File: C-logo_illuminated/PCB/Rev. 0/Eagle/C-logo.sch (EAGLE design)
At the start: 6 parts

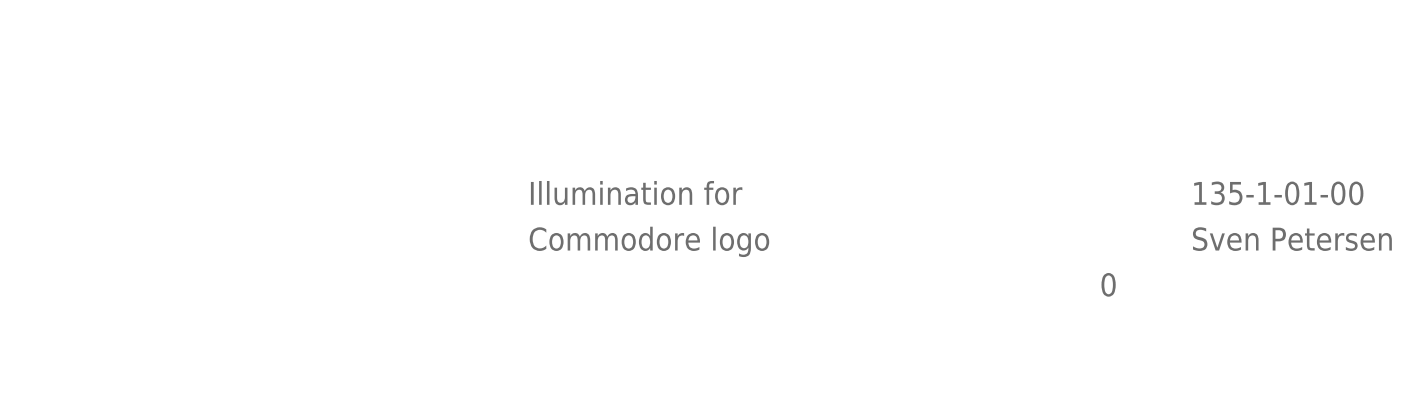
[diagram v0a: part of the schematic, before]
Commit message: Silk Screen updated
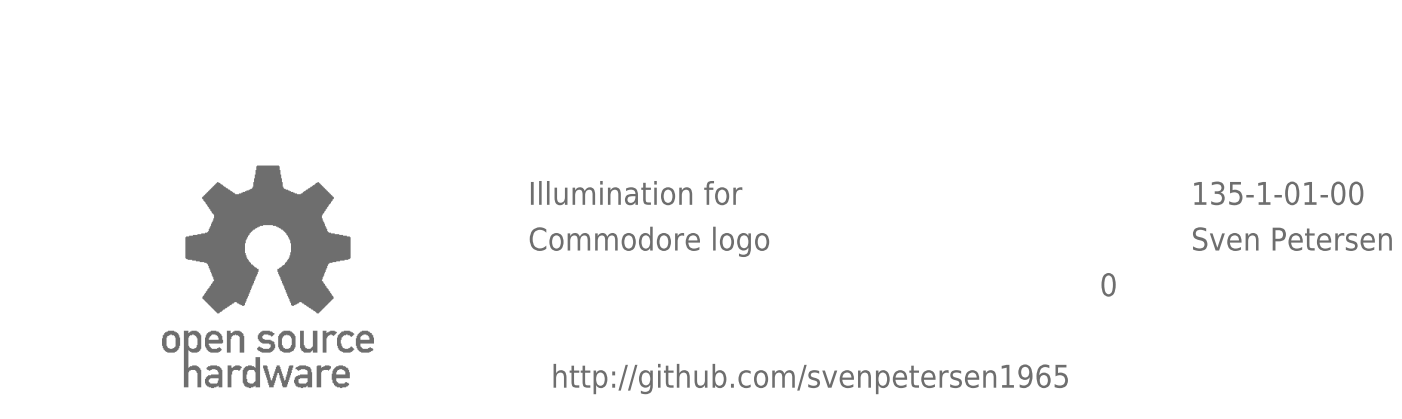
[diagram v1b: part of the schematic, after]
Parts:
- added U$5: OPEN_SOURCE_HW, Logo:OPEN_SOURCE_HW
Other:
- note added: "http://github.com/svenpetersen1965"
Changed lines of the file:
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@@
 <?xml version="1.0" encoding="utf-8"?>
 <!DOCTYPE eagle SYSTEM "eagle.dtd">
-<eagle version="9.2.2">
+<eagle version="9.5.2">
 <drawing>
 <settings>
@@
 <layer number="54" name="bGND_GNDA" color="7" fill="1" visible="no" active="no"/>
 <layer number="56" name="wert" color="7" fill="1" visible="no" active="no"/>
+<layer number="57" name="tCAD" color="7" fill="1" visible="no" active="no"/>
+<layer number="58" name="b3Ddata" color="7" fill="1" visible="no" active="no"/>
 <layer number="59" name="tCarbon" color="7" fill="1" visible="no" active="no"/>
 <layer number="60" name="bCarbon" color="7" fill="1" visible="no" active="no"/>
@@
 <layer number="97" name="Info" color="7" fill="1" visible="yes" active="yes"/>
 <layer number="98" name="Guide" color="6" fill="1" visible="yes" active="yes"/>
+<layer number="99" name="SpiceOrder" color="7" fill="1" visible="no" active="no"/>
 <layer number="100" name="Flex-Dim" color="1" fill="7" visible="no" active="no"/>
 <layer number="101" name="Flex-Kleb" color="1" fill="7" visible="no" active="no"/>
@@
 <layer number="115" name="logo4" color="7" fill="1" visible="yes" active="yes"/>
 <layer number="116" name="Patch_BOT" color="7" fill="1" visible="yes" active="yes"/>
+<layer number="117" name="BACKMAAT1" color="7" fill="1" visible="no" active="yes"/>
 <layer number="118" name="Rect_Pads" color="7" fill="1" visible="yes" active="yes"/>
+<layer number="119" name="KAP_TEKEN" color="7" fill="1" visible="no" active="yes"/>
+<layer number="120" name="120" color="7" fill="1" visible="no" active="yes"/>
 <layer number="121" name="_tsilk" color="7" fill="1" visible="yes" active="yes"/>
 <layer number="122" name="_bsilk" color="7" fill="1" visible="yes" active="yes"/>
@@
 <layer number="125" name="_tNames" color="7" fill="1" visible="no" active="no"/>
 <layer number="126" name="_bNames" color="7" fill="1" visible="no" active="no"/>
+<layer number="127" name="_tValues" color="7" fill="1" visible="no" active="yes"/>
+<layer number="128" name="_bValues" color="7" fill="1" visible="no" active="yes"/>
 <layer number="129" name="Mask" color="7" fill="1" visible="yes" active="yes"/>
+<layer number="130" name="SMDSTROOK" color="7" fill="1" visible="no" active="yes"/>
 <layer number="131" name="tAdjust" color="7" fill="1" visible="yes" active="yes"/>
 <layer number="132" name="bAdjust" color="7" fill="1" visible="yes" active="yes"/>
+<layer number="133" name="Ports" color="7" fill="1" visible="no" active="yes"/>
+<layer number="134" name="Port2" color="7" fill="1" visible="no" active="yes"/>
+<layer number="135" name="Port3" color="7" fill="1" visible="no" active="yes"/>
+<layer number="136" name="mbGlue" color="7" fill="1" visible="no" active="yes"/>
+<layer number="137" name="mtTest" color="7" fill="1" visible="no" active="yes"/>
+<layer number="138" name="mbTest" color="7" fill="1" visible="no" active="yes"/>
+<layer number="139" name="mtKeepout" color="7" fill="1" visible="no" active="yes"/>
+<layer number="140" name="mbKeepout" color="7" fill="1" visible="no" active="yes"/>
+<layer number="141" name="mtRestrict" color="7" fill="1" visible="no" active="yes"/>
+<layer number="142" name="mbRestrict" color="7" fill="1" visible="no" active="yes"/>
+<layer number="143" name="mvRestrict" color="7" fill="1" visible="no" active="yes"/>
+<layer number="144" name="Drill_legend" color="7" fill="1" visible="no" active="yes"/>
+<layer number="145" name="DrillLegend_01-16" color="2" fill="9" visible="no" active="yes"/>
+<layer number="146" name="DrillLegend_01-20" color="3" fill="9" visible="no" active="yes"/>
+<layer number="147" name="mMeasures" color="7" fill="1" visible="no" active="yes"/>
+<layer number="148" name="mDocument" color="7" fill="1" visible="no" active="yes"/>
+<layer number="149" name="mReference" color="7" fill="1" visible="no" active="yes"/>
+<layer number="150" name="Notes" color="7" fill="1" visible="no" active="yes"/>
 <layer number="151" name="L$151" color="7" fill="1" visible="no" active="no"/>
+<layer number="152" name="_bDocu" color="7" fill="1" visible="no" active="yes"/>
+<layer number="153" name="FabDoc1" color="7" fill="1" visible="no" active="yes"/>
+<layer number="154" name="FabDoc2" color="7" fill="1" visible="no" active="yes"/>
+<layer number="155" name="FabDoc3" color="7" fill="1" visible="no" active="yes"/>
+<layer number="191" name="mNets" color="7" fill="1" visible="no" active="yes"/>
+<layer number="192" name="mBusses" color="7" fill="1" visible="no" active="yes"/>
+<layer number="193" name="mPins" color="7" fill="1" visible="no" active="yes"/>
+<layer number="194" name="mSymbols" color="7" fill="1" visible="no" active="yes"/>
+<layer number="195" name="mNames" color="7" fill="1" visible="no" active="yes"/>
+<layer number="196" name="mValues" color="7" fill="1" visible="no" active="yes"/>
+<layer number="199" name="Contour" color="7" fill="1" visible="no" active="yes"/>
 <layer number="200" name="200bmp" color="7" fill="1" visible="yes" active="yes"/>
 <layer number="201" name="201bmp" color="7" fill="1" visible="yes" active="yes"/>
@@
 <layer number="226" name="226bmp" color="7" fill="1" visible="yes" active="yes"/>
 <layer number="227" name="227bmp" color="7" fill="1" visible="yes" active="yes"/>
+<layer number="228" name="228bmp" color="7" fill="1" visible="no" active="yes"/>
+<layer number="229" name="229bmp" color="7" fill="1" visible="no" active="yes"/>
+<layer number="230" name="230bmp" color="7" fill="1" visible="no" active="yes"/>
+<layer number="231" name="231bmp" color="7" fill="1" visible="no" active="yes"/>
+<layer number="232" name="Eagle3D_PG2" color="7" fill="1" visible="no" active="no"/>
+<layer number="233" name="Eagle3D_PG3" color="7" fill="1" visible="no" active="no"/>
+<layer number="248" name="Housing" color="7" fill="1" visible="no" active="yes"/>
+<layer number="249" name="Edge" color="7" fill="1" visible="no" active="yes"/>
 <layer number="250" name="Descript" color="7" fill="1" visible="yes" active="yes"/>
 <layer number="251" name="SMDround" color="7" fill="1" visible="yes" active="yes"/>
+<layer number="252" name="BR-BS" color="7" fill="1" visible="no" active="yes"/>
+<layer number="253" name="BR-LS" color="7" fill="1" visible="no" active="yes"/>
 <layer number="254" name="cooling" color="7" fill="1" visible="yes" active="yes"/>
+<layer number="255" name="routoute" color="7" fill="1" visible="no" active="yes"/>
 </layers>
 <schematic xreflabel="%F%N/%S.%C%R" xrefpart="/%S.%C%R">
@@
 <part name="+5V" library="Pads" deviceset="PAD1,0/AUTO" device=""/>
 <part name="GND" library="Pads" deviceset="PAD1,0/AUTO" device=""/>
+<part name="U$5" library="Logo" deviceset="OPEN_SOURCE_HW" device=""/>
 </parts>
 <sheets>
@@
 <text x="241.3" y="22.86" size="2.54" layer="95">Sven Petersen</text>
 <text x="231.14" y="17.78" size="2.54" layer="95">0</text>
+<text x="170.18" y="7.62" size="2.54" layer="95">http://github.com/svenpetersen1965</text>
 </plain>
 <instances>
@@
 <attribute name="NAME" x="161.925" y="97.4725" size="1.778" layer="95" ratio="10" rot="R180"/>
 </instance>
+<instance part="U$5" gate="G$1" x="127" y="7.62" smashed="yes"/>
 </instances>
 <busses>
